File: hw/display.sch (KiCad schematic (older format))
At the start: 7 parts, among them U1 4050, U3 MSP2202_2.2inch-display

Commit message: multiple changes
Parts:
- U1: value 4050 -> 74HC4050
- U3: value MSP2202_2.2inch-display -> 2.2\" SPI display
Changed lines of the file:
@@
 $EndDescr
-$Comp
-L 4xxx:4050 U?
-U 7 1 5DDDAB74
-P 3250 2550
-AR Path="/5DDDAB74" Ref="U?"  Part="7"
-AR Path="/5DDD0CFA/5DDDAB74" Ref="U1"  Part="7"
-F 0 "U1" H 3480 2596 50  0000 L CNN
-F 1 "4050" H 3480 2505 50  0000 L CNN
-F 2 "Package_SO:SOP-16_4.55x10.3mm_P1.27mm" H 3250 2550 50  0001 C CNN
-F 3 "http://www.intersil.com/content/dam/intersil/documents/cd40/cd4050bms.pdf" H 3250 2550 50  0001 C CNN
-	7    3250 2550
-	1    0    0    -1
-$EndComp
 $Comp
 L power:+3.3V #PWR?
@@
 AR Path="/5DDD0CFA/5DDE61EE" Ref="U1"  Part="1"
 F 0 "U1" H 2800 4267 50  0000 C CNN
-F 1 "4050" H 2800 4176 50  0000 C CNN
+F 1 "74HC4050" H 2800 4176 50  0000 C CNN
 F 2 "Package_SO:SOP-16_4.55x10.3mm_P1.27mm" H 2800 3950 50  0001 C CNN
 F 3 "http://www.intersil.com/content/dam/intersil/documents/cd40/cd4050bms.pdf" H 2800 3950 50  0001 C CNN
@@
 AR Path="/5DDD0CFA/5DDE61F4" Ref="U1"  Part="2"
 F 0 "U1" H 3200 4467 50  0000 C CNN
-F 1 "4050" H 3200 4376 50  0000 C CNN
+F 1 "74HC4050" H 3200 4376 50  0000 C CNN
 F 2 "Package_SO:SOP-16_4.55x10.3mm_P1.27mm" H 3200 4150 50  0001 C CNN
 F 3 "http://www.intersil.com/content/dam/intersil/documents/cd40/cd4050bms.pdf" H 3200 4150 50  0001 C CNN
@@
 AR Path="/5DDD0CFA/5DDE61FA" Ref="U1"  Part="3"
 F 0 "U1" H 2750 4667 50  0000 C CNN
-F 1 "4050" H 2750 4576 50  0000 C CNN
+F 1 "74HC4050" H 2750 4576 50  0000 C CNN
 F 2 "Package_SO:SOP-16_4.55x10.3mm_P1.27mm" H 2750 4350 50  0001 C CNN
 F 3 "http://www.intersil.com/content/dam/intersil/documents/cd40/cd4050bms.pdf" H 2750 4350 50  0001 C CNN
@@
 AR Path="/5DDD0CFA/5DED06FC" Ref="U1"  Part="4"
 F 0 "U1" H 3200 4867 50  0000 C CNN
-F 1 "4050" H 3200 4776 50  0000 C CNN
+F 1 "74HC4050" H 3200 4776 50  0000 C CNN
 F 2 "Package_SO:SOP-16_4.55x10.3mm_P1.27mm" H 3200 4550 50  0001 C CNN
 F 3 "http://www.intersil.com/content/dam/intersil/documents/cd40/cd4050bms.pdf" H 3200 4550 50  0001 C CNN
@@
 AR Path="/5DDD0CFA/5DC49FA3" Ref="U1"  Part="5"
 F 0 "U1" H 2750 5117 50  0000 C CNN
-F 1 "4050" H 2750 5026 50  0000 C CNN
+F 1 "74HC4050" H 2750 5026 50  0000 C CNN
 F 2 "Package_SO:SOP-16_4.55x10.3mm_P1.27mm" H 2750 4800 50  0001 C CNN
 F 3 "http://www.intersil.com/content/dam/intersil/documents/cd40/cd4050bms.pdf" H 2750 4800 50  0001 C CNN
@@
 AR Path="/5DDD0CFA/5DF87B81" Ref="U1"  Part="6"
 F 0 "U1" H 2950 5717 50  0000 C CNN
-F 1 "4050" H 2950 5626 50  0000 C CNN
+F 1 "74HC4050" H 2950 5626 50  0000 C CNN
 F 2 "Package_SO:SOP-16_4.55x10.3mm_P1.27mm" H 2950 5400 50  0001 C CNN
 F 3 "http://www.intersil.com/content/dam/intersil/documents/cd40/cd4050bms.pdf" H 2950 5400 50  0001 C CNN
@@
 AR Path="/5DDD0CFA/5DDE61E8" Ref="U3"  Part="1"
 F 0 "U3" H 7325 4615 50  0000 C CNN
-F 1 "MSP2202_2.2inch-display" H 7325 4524 50  0000 C CNN
+F 1 "2.2\" SPI display " H 7325 4524 50  0000 C CNN
 F 2 "display:MSP2202_2.2inch_SPI" H 7300 4100 50  0001 C CNN
 F 3 "" H 7300 4100 50  0001 C CNN
@@
 	1    0    0    -1
 $EndComp
+$Comp
+L 4xxx:4050 U?
+U 7 1 5DDDAB74
+P 3250 2550
+AR Path="/5DDDAB74" Ref="U?"  Part="7"
+AR Path="/5DDD0CFA/5DDDAB74" Ref="U1"  Part="7"
+F 0 "U1" H 3480 2596 50  0000 L CNN
+F 1 "74HC4050" H 3480 2505 50  0000 L CNN
+F 2 "Package_SO:SOP-16_4.55x10.3mm_P1.27mm" H 3250 2550 50  0001 C CNN
+F 3 "http://www.intersil.com/content/dam/intersil/documents/cd40/cd4050bms.pdf" H 3250 2550 50  0001 C CNN
+	7    3250 2550
+	1    0    0    -1
+$EndComp

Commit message: hw: pcb redesign
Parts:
- removed JP1: TFT_BL, Jumper:SolderJumper-3_P1.3mm_Bridged12_RoundedPad1.0x1.5mm_NumberLabels, symbol Jumper:Jumper_3_Bridged12
- removed JP2: TFT_VCC, Jumper:SolderJumper-3_P1.3mm_Bridged12_RoundedPad1.0x1.5mm_NumberLabels, symbol Jumper:Jumper_3_Bridged12
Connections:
- net +3V3: now also U3.1 (VCC), U3.8 (TFT_BL)
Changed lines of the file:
@@
 EESchema Schematic File Version 4
-LIBS:charger2-cache
 EELAYER 30 0
 EELAYER END
 $Descr A4 11693 8268
 encoding utf-8
-Sheet 12 15
+Sheet 12 17
 Title ""
 Date ""
@@
 L power:+3.3V #PWR0115
 U 1 1 5DECB868
-P 6200 3250
-F 0 "#PWR0115" H 6200 3100 50  0001 C CNN
-F 1 "+3.3V" H 6215 3423 50  0000 C CNN
-F 2 "" H 6200 3250 50  0001 C CNN
-F 3 "" H 6200 3250 50  0001 C CNN
-	1    6200 3250
-	1    0    0    -1
-$EndComp
-Wire Wire Line
-	6200 3250 6200 3400
+P 6600 3550
+F 0 "#PWR0115" H 6600 3400 50  0001 C CNN
+F 1 "+3.3V" H 6615 3723 50  0000 C CNN
+F 2 "" H 6600 3550 50  0001 C CNN
+F 3 "" H 6600 3550 50  0001 C CNN
+	1    6600 3550
+	1    0    0    -1
+$EndComp
 Wire Wire Line
 	6600 3850 6800 3850
@@
 Wire Wire Line
 	6600 4400 6800 4400
-$Comp
-L Jumper:Jumper_3_Bridged12 JP2
-U 1 1 5DFC465B
-P 6600 3400
-F 0 "JP2" H 6600 3604 50  0000 C CNN
-F 1 "TFT_VCC" H 6600 3513 50  0000 C CNN
-F 2 "Jumper:SolderJumper-3_P1.3mm_Bridged12_RoundedPad1.0x1.5mm_NumberLabels" H 6600 3400 50  0001 C CNN
-F 3 "~" H 6600 3400 50  0001 C CNN
-	1    6600 3400
-	1    0    0    -1
-$EndComp
 Wire Wire Line
 	6600 3550 6600 3850
-Wire Wire Line
-	6350 3400 6200 3400
-$Comp
-L power:+5V #PWR0118
-U 1 1 5DFC80C5
-P 7050 3250
-F 0 "#PWR0118" H 7050 3100 50  0001 C CNN
-F 1 "+5V" H 7065 3423 50  0000 C CNN
-F 2 "" H 7050 3250 50  0001 C CNN
-F 3 "" H 7050 3250 50  0001 C CNN
-	1    7050 3250
-	1    0    0    -1
-$EndComp
-Wire Wire Line
-	7050 3250 7050 3400
-Wire Wire Line
-	7050 3400 6850 3400
 $Comp
 L power:+3.3V #PWR0119
 U 1 1 5DFCCDCD
-P 5800 4750
-F 0 "#PWR0119" H 5800 4600 50  0001 C CNN
-F 1 "+3.3V" H 5815 4923 50  0000 C CNN
-F 2 "" H 5800 4750 50  0001 C CNN
-F 3 "" H 5800 4750 50  0001 C CNN
-	1    5800 4750
+P 6600 4500
+F 0 "#PWR0119" H 6600 4350 50  0001 C CNN
+F 1 "+3.3V" V 6600 4750 50  0000 C CNN
+F 2 "" H 6600 4500 50  0001 C CNN
+F 3 "" H 6600 4500 50  0001 C CNN
+	1    6600 4500
 	0    -1   -1   0
 $EndComp
-$Comp
-L Jumper:Jumper_3_Bridged12 JP1
-U 1 1 5DFCCDD4
-P 5800 4500
-F 0 "JP1" V 5846 4567 50  0000 L CNN
-F 1 "TFT_BL" V 5755 4567 50  0000 L CNN
-F 2 "Jumper:SolderJumper-3_P1.3mm_Bridged12_RoundedPad1.0x1.5mm_NumberLabels" H 5800 4500 50  0001 C CNN
-F 3 "~" H 5800 4500 50  0001 C CNN
-	1    5800 4500
-	0    -1   -1   0
-$EndComp
-$Comp
-L power:+5V #PWR0155
-U 1 1 5DFCCDDB
-P 5800 4250
-F 0 "#PWR0155" H 5800 4100 50  0001 C CNN
-F 1 "+5V" H 5815 4423 50  0000 C CNN
-F 2 "" H 5800 4250 50  0001 C CNN
-F 3 "" H 5800 4250 50  0001 C CNN
-	1    5800 4250
-	1    0    0    -1
-$EndComp
-Wire Wire Line
-	5950 4500 6800 4500
 Text Label 6600 4300 2    50   ~ 0
 3.3_MOSI
@@
 	1    0    0    -1
 $EndComp
+Wire Wire Line
+	6600 4500 6800 4500
 $EndSCHEMATC

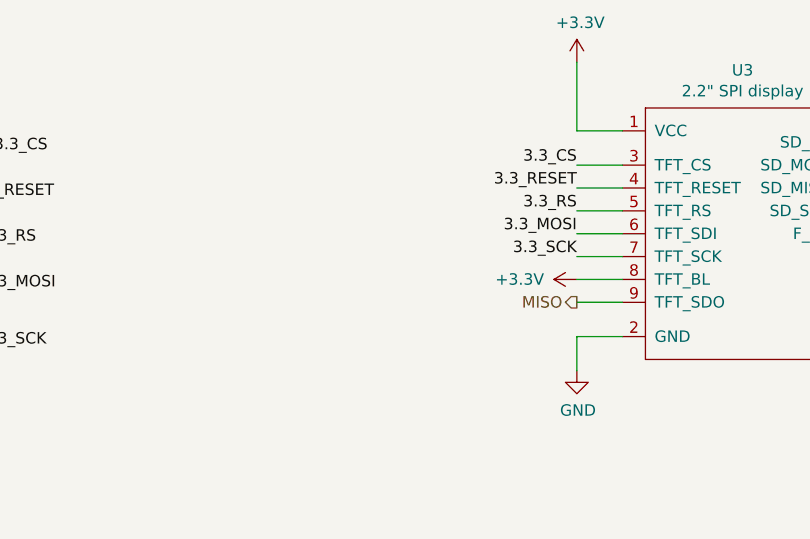
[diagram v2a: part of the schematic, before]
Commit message: additional caps, groundplane improvements, MISO 3.3->5V
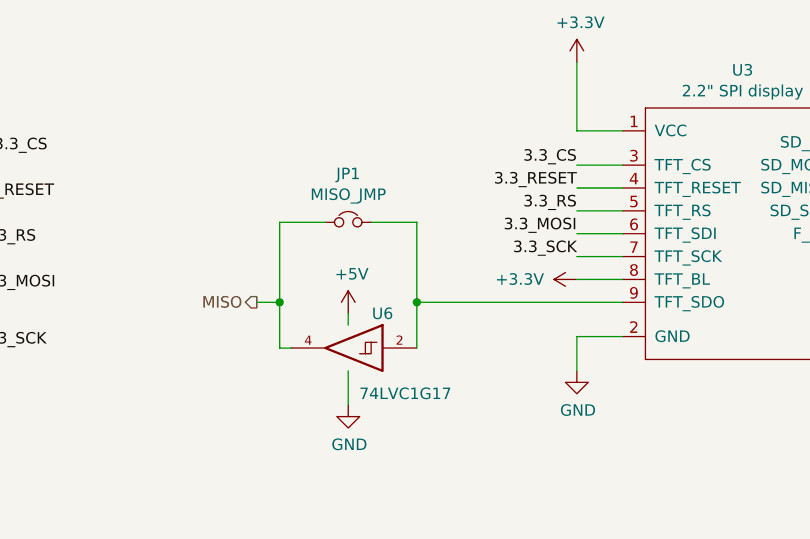
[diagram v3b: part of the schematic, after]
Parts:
- added JP1: MISO_JMP, Jumper:SolderJumper-2_P1.3mm_Bridged_RoundedPad1.0x1.5mm, symbol Device:Jumper_NC_Small
- added U6: 74LVC1G17, Package_TO_SOT_SMD:SOT-23-5, symbol 74xGxx:74LVC1G17
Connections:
- net GND: now also U6.3 (GND)
- net MISO: now also JP1.1, U6.4; no longer U3.9 (TFT_SDO)
- new net: JP1.2, U3.9 (TFT_SDO), U6.2
- new net +5V: U6.5 (VCC)
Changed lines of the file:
@@
 Wire Wire Line
 	6600 4200 6800 4200
-Text HLabel 6600 4600 0    50   Output ~ 0
+Text HLabel 5200 4600 0    50   Output ~ 0
 MISO
-Wire Wire Line
-	6600 4600 6800 4600
 Wire Wire Line
 	6600 4400 6800 4400
@@
 Wire Wire Line
 	6600 4500 6800 4500
+$Comp
+L 74xGxx:74LVC1G17 U6
+U 1 1 5FE72031
+P 5600 4800
+F 0 "U6" H 5450 4950 50  0000 C CNN
+F 1 "74LVC1G17" H 5350 4600 50  0000 C CNN
+F 2 "Package_TO_SOT_SMD:SOT-23-5" H 5600 4800 50  0001 C CNN
+F 3 "http://www.ti.com/lit/sg/scyt129e/scyt129e.pdf" H 5600 4800 50  0001 C CNN
+	1    5600 4800
+	-1   0    0    -1
+$EndComp
+$Comp
+L power:GND #PWR06
+U 1 1 5FE78A44
+P 5600 5050
+F 0 "#PWR06" H 5600 4800 50  0001 C CNN
+F 1 "GND" H 5605 4877 50  0000 C CNN
+F 2 "" H 5600 5050 50  0001 C CNN
+F 3 "" H 5600 5050 50  0001 C CNN
+	1    5600 5050
+	1    0    0    -1
+$EndComp
+Wire Wire Line
+	5600 5050 5600 4900
+$Comp
+L Device:Jumper_NC_Small JP1
+U 1 1 5FE7E428
+P 5600 4250
+F 0 "JP1" H 5600 4462 50  0000 C CNN
+F 1 "MISO_JMP" H 5600 4371 50  0000 C CNN
+F 2 "Jumper:SolderJumper-2_P1.3mm_Bridged_RoundedPad1.0x1.5mm" H 5600 4250 50  0001 C CNN
+F 3 "~" H 5600 4250 50  0001 C CNN
+	1    5600 4250
+	1    0    0    -1
+$EndComp
+Wire Wire Line
+	5900 4800 5900 4600
+Wire Wire Line
+	5900 4250 5700 4250
+Wire Wire Line
+	5300 4800 5300 4600
+Wire Wire Line
+	5300 4250 5500 4250
+Wire Wire Line
+	5350 4800 5300 4800
+$Comp
+L power:+5V #PWR05
+U 1 1 5FE89286
+P 5600 4650
+F 0 "#PWR05" H 5600 4500 50  0001 C CNN
+F 1 "+5V" H 5615 4823 50  0000 C CNN
+F 2 "" H 5600 4650 50  0001 C CNN
+F 3 "" H 5600 4650 50  0001 C CNN
+	1    5600 4650
+	1    0    0    -1
+$EndComp
+Wire Wire Line
+	5600 4650 5600 4700
+Wire Wire Line
+	5200 4600 5300 4600
+Connection ~ 5300 4600
+Wire Wire Line
+	5300 4600 5300 4250
+Wire Wire Line
+	5900 4600 6800 4600
+Connection ~ 5900 4600
+Wire Wire Line
+	5900 4600 5900 4250
 $EndSCHEMATC
